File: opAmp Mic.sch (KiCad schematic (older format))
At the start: 23 parts, among them J1 XLR3, U1 OPA2134

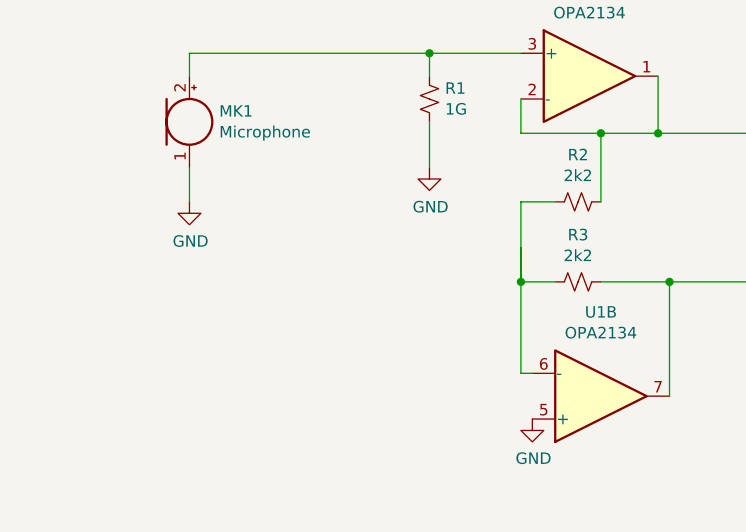
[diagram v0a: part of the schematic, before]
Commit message: moved op amp, changed current paths , enlarged and shortened high impedence nets
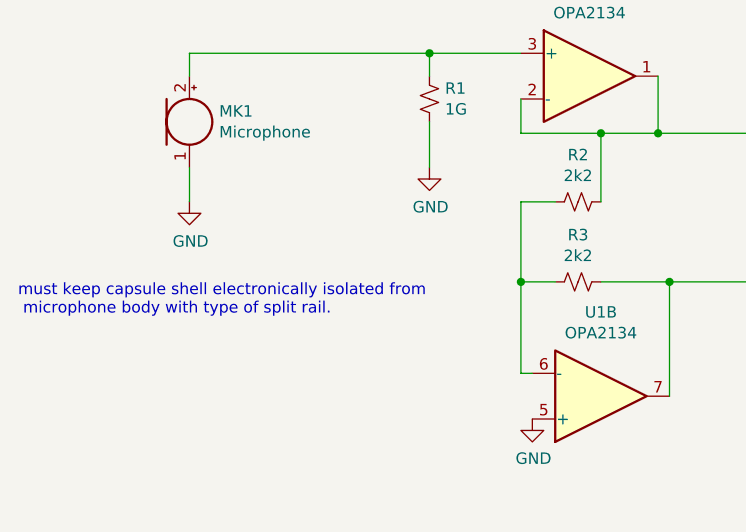
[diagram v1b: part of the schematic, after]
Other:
- note added: "must keep capsule shell electronically isolated from\n microphone body with type of split rail."
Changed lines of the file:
@@
 	3100 3200 2950 3200
 Wire Wire Line
-	2950 3550 3100 3550
-Wire Wire Line
 	2950 3950 3000 3950
-Connection ~ 2950 3550
-Wire Wire Line
-	2950 3400 2950 3550
 Wire Wire Line
 	2950 3550 2950 3950
-Wire Wire Line
-	2950 3200 2950 3550
 Wire Wire Line
 	3600 4050 3600 3550
@@
 Text Notes 7600 4550 0    50   ~ 0
 soldered on connector
+Wire Wire Line
+	2950 3200 2950 3550
+Connection ~ 2950 3550
+Wire Wire Line
+	2950 3550 3100 3550
+Text Notes 750  3700 0    50   ~ 0
+must keep capsule shell electronically isolated from\n microphone body with type of split rail.
 $EndSCHEMATC

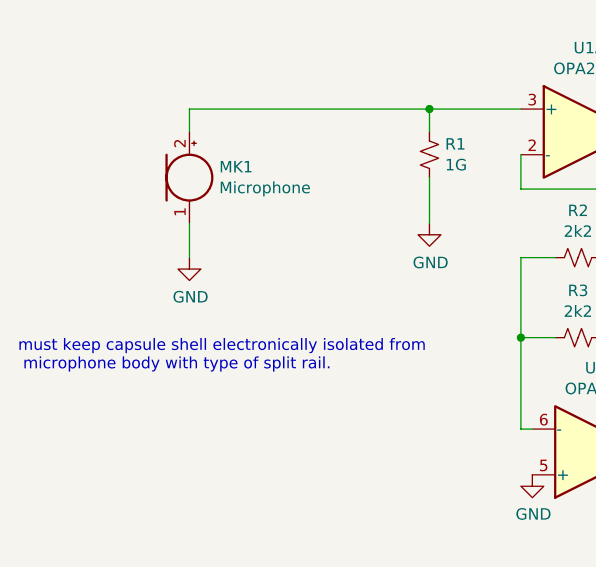
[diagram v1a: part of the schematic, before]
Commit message: made the capsule ground sit on the chassis rather than the virtual ground, which solves some of the issues I had with the initial pcb run
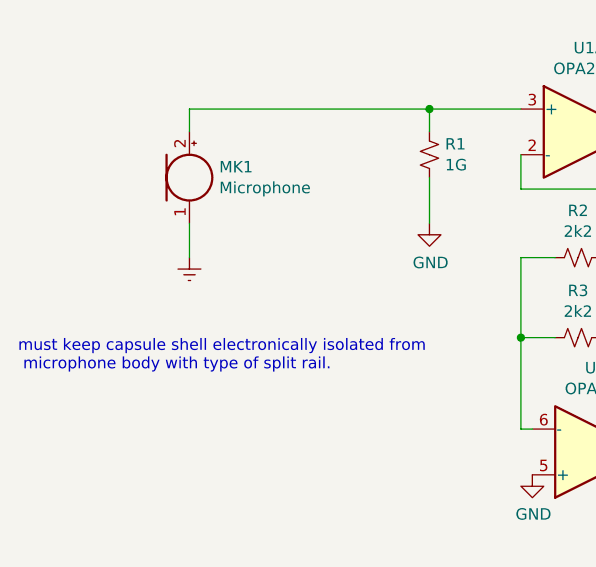
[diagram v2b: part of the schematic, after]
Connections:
- net Earth: now also MK1.1 (-)
- net GND: no longer MK1.1 (-)
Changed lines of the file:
@@
 Wire Wire Line
 	3850 1550 3850 1350
-$Comp
-L power:GND #PWR0101
-U 1 1 6082E045
-P 1500 3200
-F 0 "#PWR0101" H 1500 2950 50  0001 C CNN
-F 1 "GND" H 1505 3027 50  0000 C CNN
-F 2 "" H 1500 3200 50  0001 C CNN
-F 3 "" H 1500 3200 50  0001 C CNN
-	1    1500 3200
-	1    0    0    -1
-$EndComp
 Wire Wire Line
 	2950 2550 2550 2550
@@
 Text Notes 750  3700 0    50   ~ 0
 must keep capsule shell electronically isolated from\n microphone body with type of split rail.
+$Comp
+L power:Earth #PWR0101
+U 1 1 60F4DA44
+P 1500 3200
+F 0 "#PWR0101" H 1500 2950 50  0001 C CNN
+F 1 "Earth" H 1500 3050 50  0001 C CNN
+F 2 "" H 1500 3200 50  0001 C CNN
+F 3 "~" H 1500 3200 50  0001 C CNN
+	1    1500 3200
+	1    0    0    -1
+$EndComp
 $EndSCHEMATC

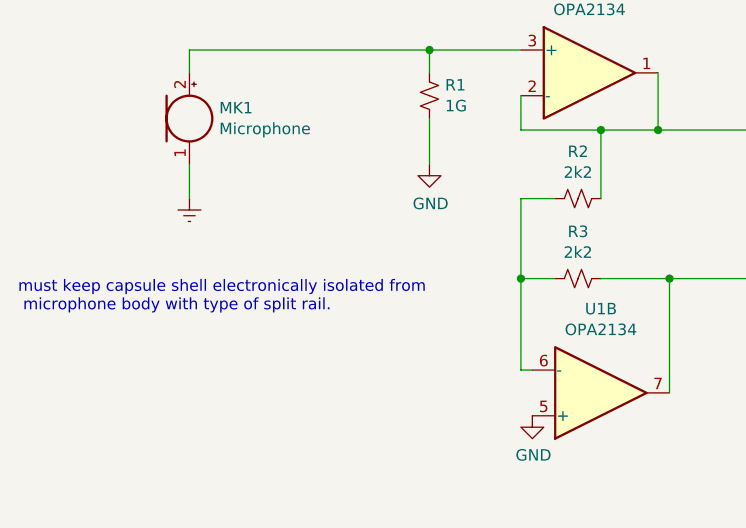
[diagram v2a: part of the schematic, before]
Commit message: cleaned up some text in the schematic
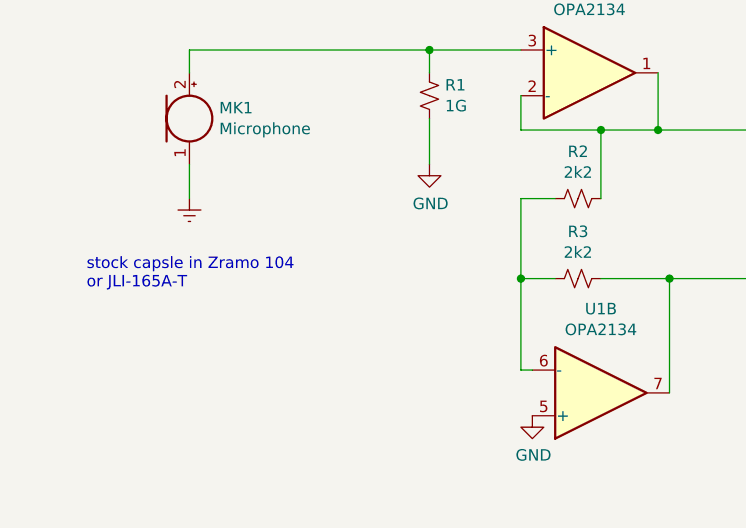
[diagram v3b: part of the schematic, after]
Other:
- note added: "stock capsle in Zramo 104\nor JLI-165A-T"
- note removed: "must keep capsule shell electronically isolated from\n microphone body with type of split rail."
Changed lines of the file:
@@
 Wire Wire Line
 	2950 3550 3100 3550
-Text Notes 750  3700 0    50   ~ 0
-must keep capsule shell electronically isolated from\n microphone body with type of split rail.
 $Comp
 L power:Earth #PWR0101
@@
 	1    0    0    -1
 $EndComp
+Text Notes 1050 3600 0    50   ~ 0
+stock capsle in Zramo 104\nor JLI-165A-T
 $EndSCHEMATC
